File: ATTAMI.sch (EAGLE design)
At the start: 31 parts, among them Q1 NTD3055L, Q2 NTD3055L, Q3 NTD3055L, U1 NCP4626 (5V), U2 ATTINY85

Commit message: ver05 friday session
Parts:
- removed BATT1: FKIT-COIN_CELLLIR2450-H, SparkFun:FKIT-COIN_CELLLIR2450-H
- removed C2: 4.7uf, SparkFun:CAP0805
- removed D2: Schottky, microbuilder:DIODESMA
- removed JP4: USB_MICROB_PLUG-SMT, SparkFun:USB_MICROB_PLUG-SMT
- removed LSP1, LSP2: LSP10, solpad:LSP10
- removed SJ1: Solder_Jumper, SparkFun:SOLDERJUMPERNC2
- added J1: (no value), Molex-47346-0001:47346-0001
- added JP7: (no value), microbuilder:HEADER-1X376MIL
- added SW1: SPST_TACT-KMR2, adafruit:SPST_TACT-KMR2
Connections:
- removed net N$2: JP1.2, R6.2, U2.PB1(MISO)
- removed net V_COIN_CELL: BATT1.POS, D2.A, SJ1.2
- net GND: now also J1.5, JP2.6, JP7.1, JP7.3, SW1.P, SW1.P1; no longer BATT1.NEG, C2.2, JP2.7, JP4.GND, LSP2.MP
- net N$10: now also J1.2; no longer JP4.D-
- net N$15: now also JP1.2, R6.2, U2.PB1(MISO)
- net N$7: now also J1.3; no longer JP4.D+
- net N$8: now also SW1.S, SW1.S1
- net VCC: now also JP2.5; no longer C2.1, D2.C, SJ1.1
- net V_BAT: now also JP7.2; no longer LSP1.MP
- net V_USB: now also J1.1; no longer JP4.VCC
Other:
- note added: "Notes for the PCB editor: 1. U1 part # is NCP4626HSN050T1G see data sheet for package details 2. Vin, ECO and CE pins of U1 "NCP4626" should be connected. 3. U1 ground trace should be large enough for heat dissipation (also use some VIAs to transfer heat to the other side of the board). 4. C1 should be placed as close as possible to U1. 5. C3 and C4 should be placed as close as possible to U2. No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"
- note added: "TAMI-ATTINY-V05.sch 09-05-2014 21:52"
- note removed: "Notes for the PCB editor: 1. U1 part # is NCP4626HSN050T1G see data sheet for package details 2. Vin, ECO and CE pins of U1 "NCP4626" should be connected. 3. U1 ground trace should be large enough for heat dissipation (also use some VIAs to transfer heat to the other side of the board). 4. C1 and C2 should be placed as close as possible to U1. 5. C3 and C4 should be placed as close as possible to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"
- note removed: "TAMI-ATTINY-V04.sch 30-04-2014 21:52"
- moved on the sheet: JP2, R7

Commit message: ver07
https://dl.dropboxusercontent.com/u/6430706/ShareX/2014/05/TAMI-ATTINY-V07.pdf
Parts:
- removed C1: 4.7uf, SparkFun:CAP0805
- removed D6: Red LED, SparkFun:LED0603
- removed D7: Green LED, SparkFun:LED0603
- removed D8: Blue LED, SparkFun:LED0603
- removed JP2: (no value), SparkFun:M07
- removed JP7: (no value), microbuilder:HEADER-1X376MIL
- removed Q1, Q2, Q3: NTD3055L, transistor-small-signal:BSS123
- removed R5: 560R, SparkFun:RESISTOR0402-RES
- removed R6, R7: 330R, SparkFun:RESISTOR0402-RES
- added C2: 4.7uf, SparkFun:CAP0805
- added J2, J3: CON_HEADER_1X05-PTH, dp_devices:CON_HEADER_1X05-PTH
- C4: device SparkFun:CAP0402-CAP -> SparkFun:CAP0805
- D1: device microbuilder:DIODESMA -> microbuilder:DIODESOD-323
- D3, D4, D5: device SparkFun:LED0603 -> dp_devices:LED-0805
- JP1: device SparkFun:M07 -> microbuilder:HEADER-1X376MIL
- R1, R2, R3, R4: device SparkFun:RESISTOR0402-RES -> SparkFun:RESISTOR0805-RES
- U1: value NCP4626 (5V) -> NCP4626; device v-reg:LP2950CDT-3.0 -> yair_r:NCP4626
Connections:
- removed net N$12: D7.A, R6.1
- removed net N$13: D6.A, R5.1
- removed net N$14: D8.A, R7.1
- removed net N$16: JP2.3, Q3.D
- removed net N$4: JP2.2, Q2.D
- removed net N$9: JP2.1, Q1.D
- net GND: now also C2.2, J2.5, J3.5, JP1.1, JP1.3; no longer C1.2, D6.C, D7.C, D8.C, JP1.7, JP2.4, JP2.6, JP7.1, JP7.3, Q1.S, Q2.S, Q3.S
- net N$1: now also J3.1; no longer JP1.4
- net N$15: now also J2.2; no longer JP1.2, Q2.G, R6.2
- net N$3: now also J2.1; no longer JP1.1, Q1.G, R5.2
- net N$5: now also J2.3; no longer JP1.3, Q3.G, R7.2
- net N$6: now also J3.2; no longer JP1.5
- net N$8: now also J3.3; no longer JP1.6
- net VCC: now also J2.4, U1.VOUT; no longer JP2.5, U1.OUT
- net V_BAT: now also C2.1, J3.4, JP1.2, U1.ECO, U1.EN, U1.VIN; no longer C1.1, JP7.2, U1.IN
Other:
- note added: "Notes for the PCB editor: 1. U1 ground trace should be large enough for heat dissipation (also use some VIAs to transfer heat to the other side of the board). 2. C1 should be placed as close as possible to U1. 3. C3 and C4 should be placed as close as possible to U2. Notes for the USER: 1. D3, D4 and D5 are Blue and/or Green LEDs they might not light when using Vin <4V~ power source 2. When VCC i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"
- note added: "T.A.M.I hackerspace crew LICENSE: CERN OHL 1.7"
- note removed: "Notes for the PCB editor: 1. U1 part # is NCP4626HSN050T1G see data sheet for package details 2. Vin, ECO and CE pins of U1 "NCP4626" should be connected. 3. U1 ground trace should be large enough for heat dissipation (also use some VIAs to transfer heat to the other side of the board). 4. C1 should be placed as close as possible to U1. 5. C3 and C4 should be placed as close as possible to U2. No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"
- note removed: "TAMI-ATTINY-V05.sch 09-05-2014 21:52"
- moved on the sheet: C3, C4, D1, J1, R1, R2, R3, R4, SW1, U2

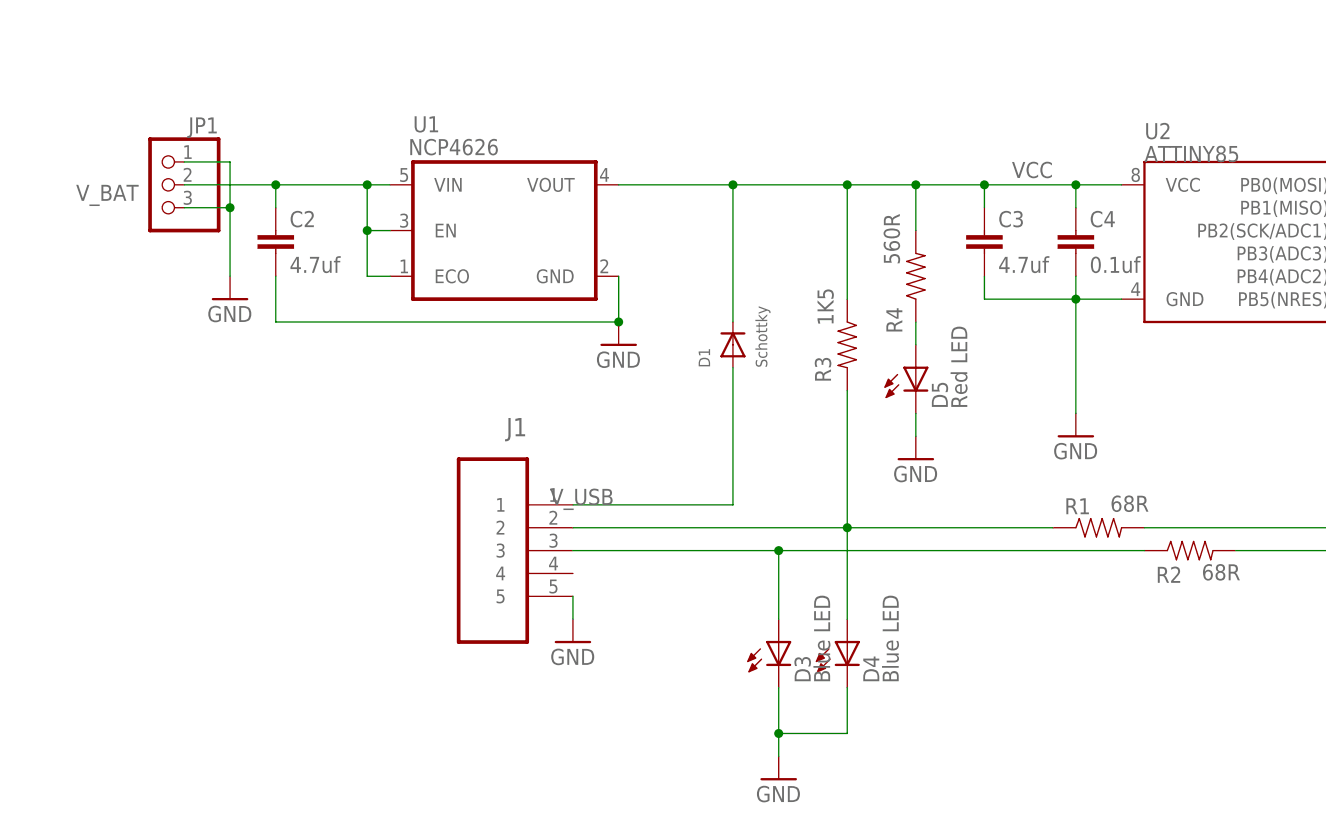
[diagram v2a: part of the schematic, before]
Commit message: ver08
[zvi] switched the LDO to MIC5225. also changed some capacitors.
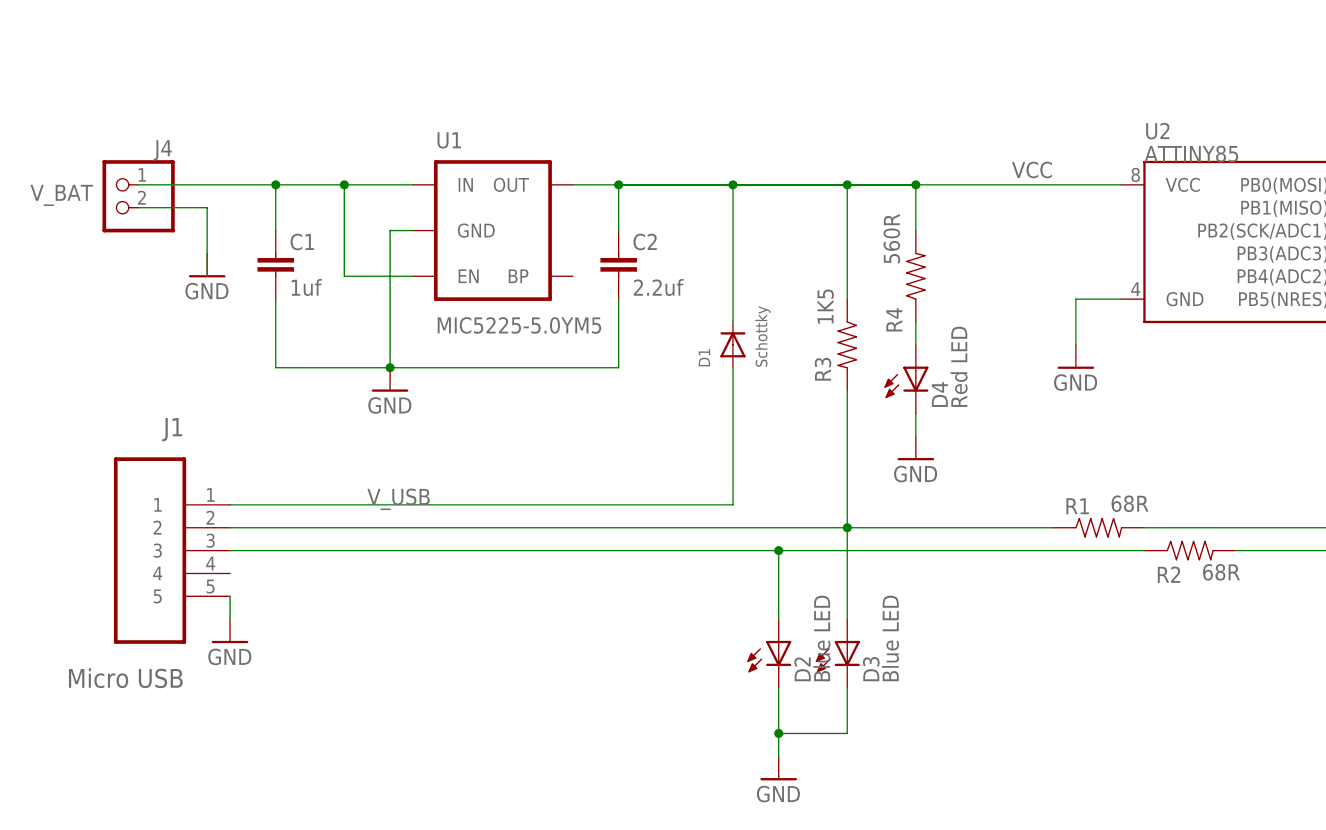
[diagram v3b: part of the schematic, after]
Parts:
- removed C3: 4.7uf, SparkFun:CAP0805
- removed C4: 0.1uf, SparkFun:CAP0805
- removed D5: Red LED, dp_devices:LED-0805
- removed JP1: (no value), microbuilder:HEADER-1X376MIL
- added C1: 1uf, SparkFun:CAP0805
- added D2: Blue LED, dp_devices:LED-0805
- added J4: (no value), pinhead:PINHD-1X2
- C2: value 4.7uf -> 2.2uf
- D4: value Blue LED -> Red LED
- J1: value (none) -> Micro USB
- U1: value NCP4626 -> MIC5225-5.0YM5; device yair_r:NCP4626 -> SparkFun:V_REG_LDOSMD
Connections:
- new net N$4: J4.2
- net GND: now also C1.2, D2.C; no longer C3.2, C4.2, D5.C, JP1.1, JP1.3
- net N$10: now also D3.A; no longer D4.A
- net N$11: now also D4.A; no longer D5.A
- net N$7: now also D2.A; no longer D3.A
- net VCC: now also C2.1, U1.OUT; no longer C3.1, C4.1, U1.VOUT
- net V_BAT: now also C1.1, J4.1, U1.IN; no longer C2.1, JP1.2, U1.ECO, U1.VIN
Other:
- note added: "AT TAMI Ver. 8"
- note added: "Notes for the PCB editor: 1. U1 ground trace should be large enough for heat dissipation (also use some VIAs to transfer heat to the other side of the board). 2. C1 should be placed as close as possible to U1. 3. C2 should be placed as close as possible to U1. Notes for the USER: 1. D2 and D3 are Blue LEDs they might not light when using Vi_BAT <4V~ 2. When VCC is less than 5V change the system c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"
- note removed: "Notes for the PCB editor: 1. U1 ground trace should be large enough for heat dissipation (also use some VIAs to transfer heat to the other side of the board). 2. C1 should be placed as close as possible to U1. 3. C3 and C4 should be placed as close as possible to U2. Notes for the USER: 1. D3, D4 and D5 are Blue and/or Green LEDs they might not light when using Vin <4V~ power source 2. When VCC i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"
- moved on the sheet: C2, D3, D4, J1

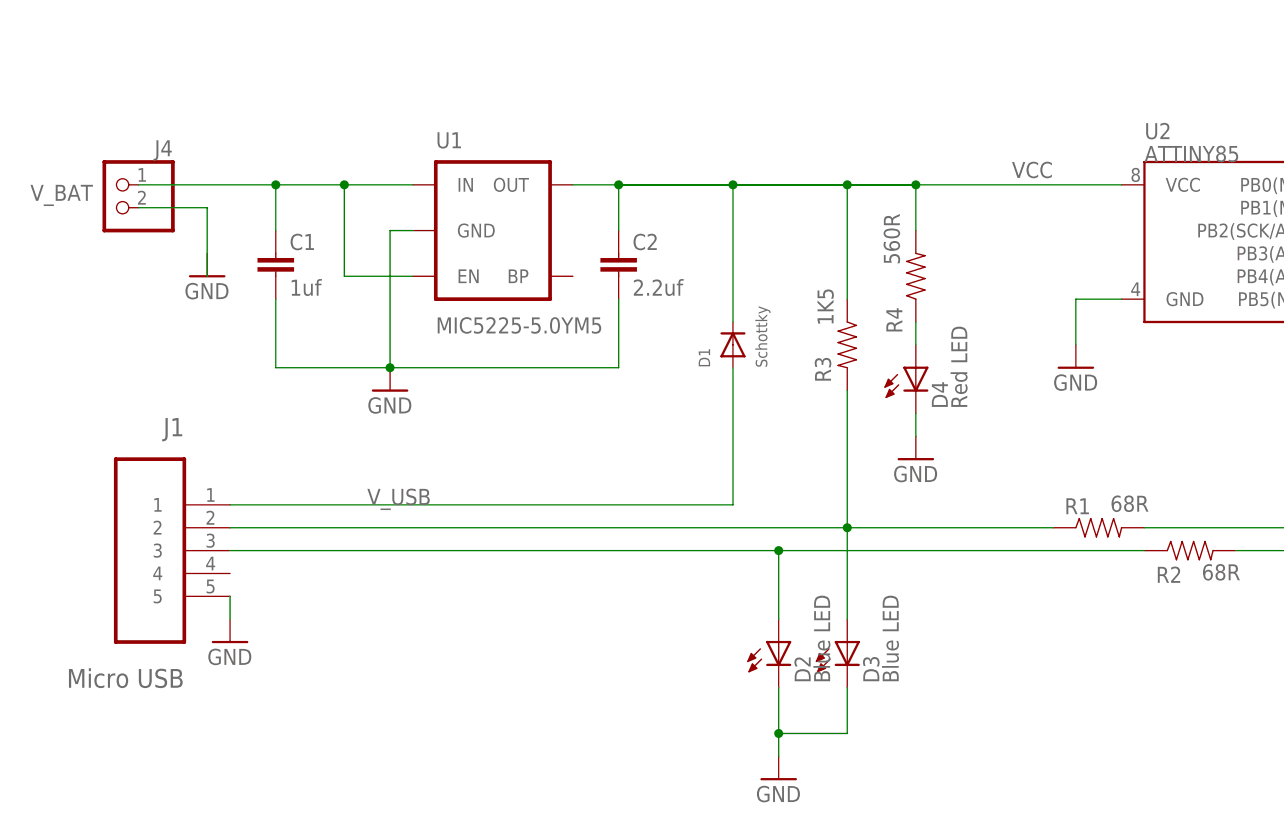
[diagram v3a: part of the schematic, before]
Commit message: ver 09
[zvi] changed the schematics. MIC5205 is in together with its capacitor C3.
The MIC5205 has two drawbacks:
  a. No guaranteed behavior for Vin < 5.5 V.  
  b. No guaranteed behavior regarding reverse leakage.
For applications with external supply greater than 5.5V there is no problem.
We will have to test the reverse current issue when operating on USB 5V without external supply.
We will have to test the dropout issue when operating on external supply lower than 5.5V.
Anyhow we will be able to switch back to the MIC5225 without changing the PCB.
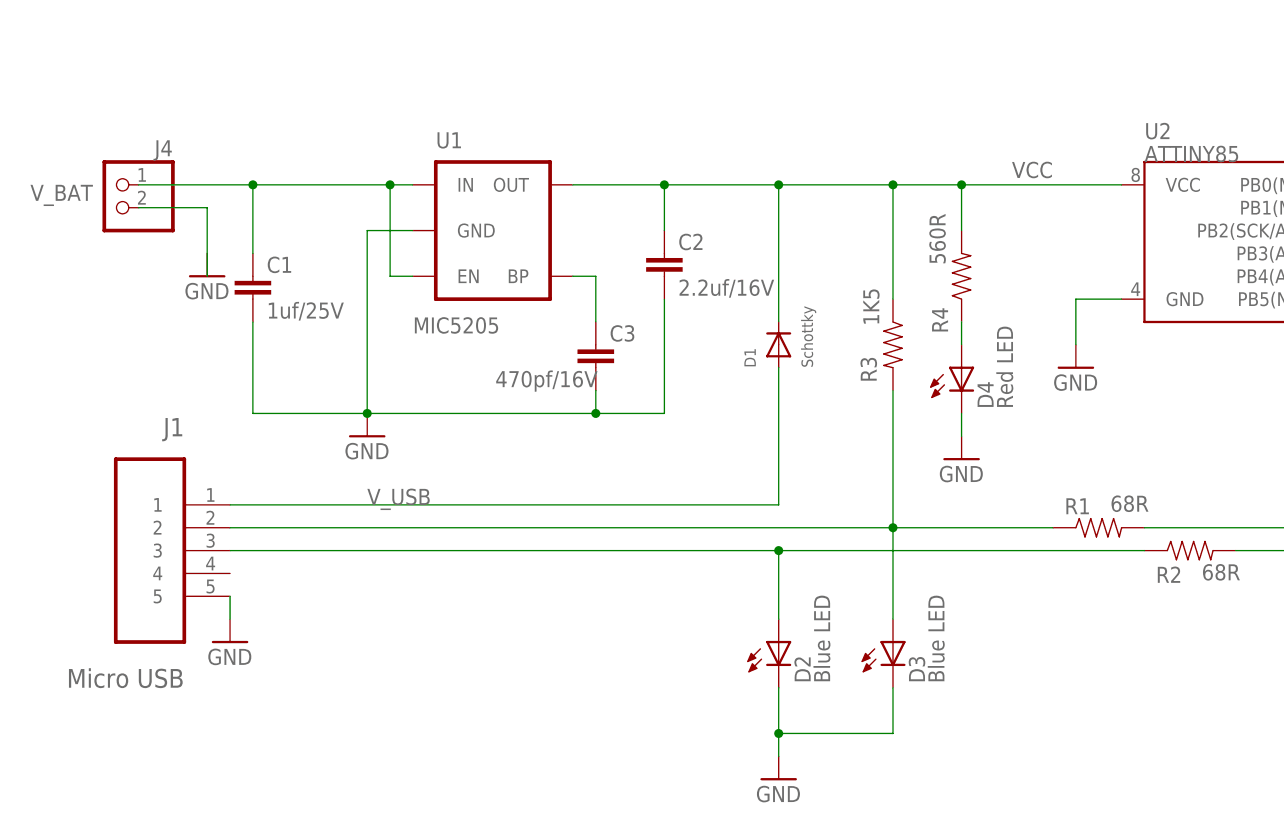
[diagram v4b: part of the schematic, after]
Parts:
- added C3: 470pf/16V, SparkFun:CAP0805
- C1: value 1uf -> 1uf/25V
- C2: value 2.2uf -> 2.2uf/16V
- U1: value MIC5225-5.0YM5 -> MIC5205
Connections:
- new net N$9: C3.1, U1.BP
- net GND: now also C3.2
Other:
- moved on the sheet: C1, C2, D1, D3, D4, R3, R4

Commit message: ver 12
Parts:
- removed C2: 2.2uf/16V, SparkFun:CAP0805
- removed SW1: SPST_TACT-KMR2, adafruit:SPST_TACT-KMR2
- added S1: SWITCH-MOMENTARY-2-SMD-1101NE, SparkFun-Electromechanical:SWITCH-MOMENTARY-2-SMD-1101NE
- added U$1: MOUNTINGHOLE2.0, microbuilder:MOUNTINGHOLE2.0
- C3: value 470pf/16V -> 2.2uf/16V
- D1: value Schottky -> Blue LED; device microbuilder:DIODESOD-323 -> dp_devices:LED-0805
- D3: value Blue LED -> Schottky; device dp_devices:LED-0805 -> microbuilder:DIODESOD-323
- J1: value Micro USB -> CON_HEADER_1X02-PTH; device Molex-47346-0001:47346-0001 -> dp_devices:CON_HEADER_1X02-PTH
- J2: value CON_HEADER_1X05-PTH -> MICRO-USB_ALIEXPRESS; device dp_devices:CON_HEADER_1X05-PTH -> yair_r:MICRO-USB_ALIEXPRESS
- J4: value (none) -> CON_HEADER_1X05-PTH; device pinhead:PINHD-1X2 -> dp_devices:CON_HEADER_1X05-PTH
- R1: value 68R -> 1K5
- R2: value 68R -> 560R
- R3: value 1K5 -> 68R
- R4: value 560R -> 68R
- U1: value MIC5205 -> MIC5225
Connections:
- removed net N$4: J4.2
- removed net N$9: C3.1, U1.BP
- removed net V_USB: D1.A, J1.1
- new net N$2: D3.A, J2.VCC
- net GND: now also D1.C, J1.2, J2.GND@1, J2.GND@2, J2.GND@3, J4.5, S1.1; no longer C2.2, D3.C, J1.5, J2.5, SW1.P, SW1.P1
- net N$1: now also J4.1, R3.2; no longer J3.1, R1.2
- net N$10: now also D2.A, J2.DM, R1.2, R3.1; no longer D3.A, J1.2, R1.1, R3.2
- net N$11: now also R2.1; no longer R4.1
- net N$15: now also J3.2; no longer J2.2
- net N$3: now also J3.1; no longer J2.1
- net N$5: now also J3.3; no longer J2.3
- net N$6: now also J4.2, R4.2; no longer J3.2, R2.2
- net N$7: now also D1.A, J2.DP, R4.1; no longer D2.A, J1.3, R2.1
- net N$8: now also J4.3, S1.2; no longer J3.3, SW1.S, SW1.S1
- net VCC: now also C3.1, D3.C, J3.4, R1.1, R2.2; no longer C2.1, D1.C, J2.4, R3.1, R4.2
- net V_BAT: now also J1.1, J4.4; no longer J3.4, J4.1
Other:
- note added: "AT TAMI Ver. 9b"
- note added: "Notes for the PCB editor: 1. U1 ground trace should be large enough for heat dissipation (also use some VIAs to transfer heat to the other side of the board). 2. C1 should be placed as close as possible to U1. 3. C3 should be placed as close as possible to U1. Assembley notes: Don't populate C2 if you use MIC5225. only populate it if you use MIC5205 instead of MIC5225. Notes for the USER: 1. D2 a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"
- note removed: "AT TAMI Ver. 8"
- note removed: "Notes for the PCB editor: 1. U1 ground trace should be large enough for heat dissipation (also use some VIAs to transfer heat to the other side of the board). 2. C1 should be placed as close as possible to U1. 3. C2 should be placed as close as possible to U1. Notes for the USER: 1. D2 and D3 are Blue LEDs they might not light when using Vi_BAT <4V~ 2. When VCC is less than 5V change the system c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"
- moved on the sheet: C3, D2, J3, R1, R2, R3, R4

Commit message: ver 15b
this could be printed....
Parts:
- added U$2: MOUNTINGHOLE2.0, microbuilder:MOUNTINGHOLE2.0
- J3: value CON_HEADER_1X05-PTH -> CON_HEADER_1X02-PTH; device dp_devices:CON_HEADER_1X05-PTH -> dp_devices:CON_HEADER_1X02-PTH
- J4: value CON_HEADER_1X05-PTH -> (none); device dp_devices:CON_HEADER_1X05-PTH -> adafruit:PINHD-1X6CB
- renumbered C3 to C2
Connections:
- net N$2 renamed V-BUS
- net GND: now also J3.2; no longer J3.5, J4.5
- net N$1: now also J4.4; no longer J4.1
- net N$15: now also J4.2; no longer J3.2
- net N$3: now also J4.1; no longer J3.1
- net N$5: now also J4.3; no longer J3.3
- net N$6: now also J4.5; no longer J4.2
- net N$8: now also J4.6; no longer J4.3
- net VCC: now also J3.1; no longer J3.4
- net V_BAT: no longer J4.4
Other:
- note added: "AT TAMI Ver. 15b"
- note added: "Notes: 1. D2 and D3 are Blue LEDs they might not light when using Vi_BAT <4V~ 2. When VCC is less than 5V change the system clock of the ATTINY85 to 8MHz or less (refer to datasheet of P163 speed figure 21-1)"
- note removed: "AT TAMI Ver. 9b"
- note removed: "Notes for the PCB editor: 1. U1 ground trace should be large enough for heat dissipation (also use some VIAs to transfer heat to the other side of the board). 2. C1 should be placed as close as possible to U1. 3. C3 should be placed as close as possible to U1. Assembley notes: Don't populate C2 if you use MIC5225. only populate it if you use MIC5205 instead of MIC5225. Notes for the USER: 1. D2 a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"
- moved on the sheet: J1
